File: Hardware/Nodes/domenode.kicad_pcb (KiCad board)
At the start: 2 copper layers, 100 x 70 mm, 89 parts, among them J1 MIC_JUMPER, J10 5V, J11 TOUCH, J12 24V, J13 CAN_BOARD, J15 RGB_SHIELD, J16 RGB_SHIELD, J17 GROVE/I2C, J18 ISP, J19 CAN_IN, J2 MIC_HEADER, J20 CAN_OUT, J21 SWITCHES, J3 SW0, J4 CANTERM, J5 3V3, J6 POWER_TEST, J9 SENSOR, Q1 MMBT918 (2N706 equiv), Q2 MMBT2222A (2N2222 equiv), SW1 SW1, SW2 SW2, SW3 RESET, SW4 BOOT, U1 MINI-360, U2 AMS1117-3.3, U3 ESP32-WROOM, U5 TSDP341xx, U6 SN65HVD230

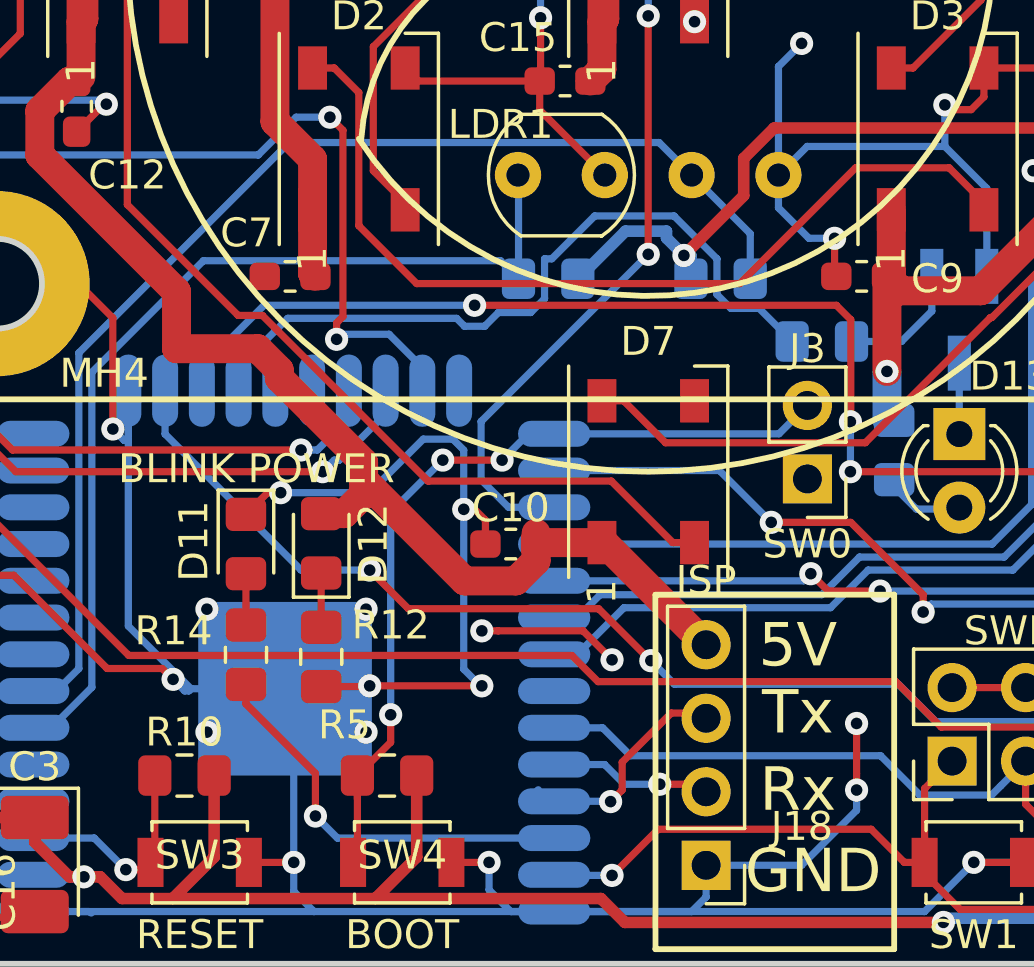
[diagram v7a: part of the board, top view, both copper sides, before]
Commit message: added LDR models
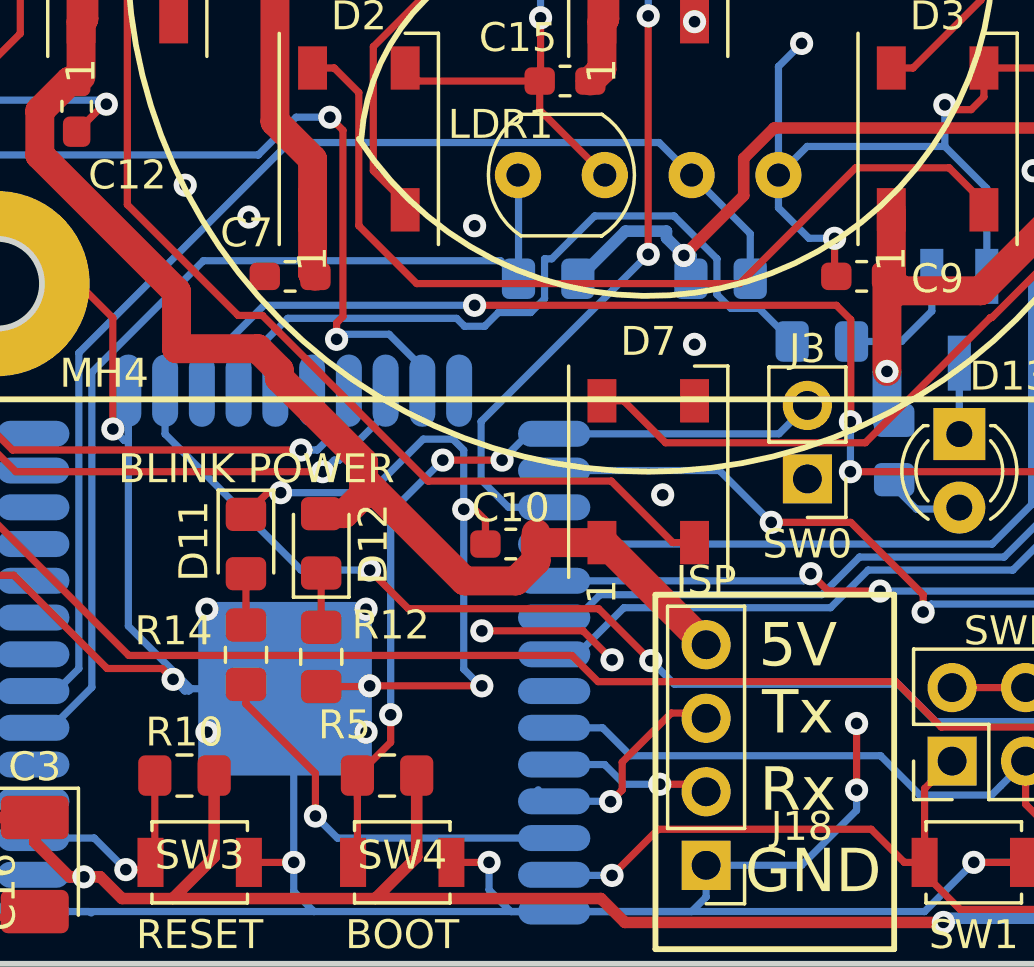
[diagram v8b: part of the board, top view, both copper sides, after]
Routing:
- net CANGND: vias 34 -> 39
